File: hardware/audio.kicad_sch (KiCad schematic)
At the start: 35 parts, among them J4 NCJ6FA-H-0, J5 NCJ6FA-H-0, J6 Conn_01x04_Pin, J7 NCJ6FA-H-0, J8 NCJ6FA-H-0, U5 THAT1246, U6 THAT1246, U7 THAT1646, U8 THAT1646

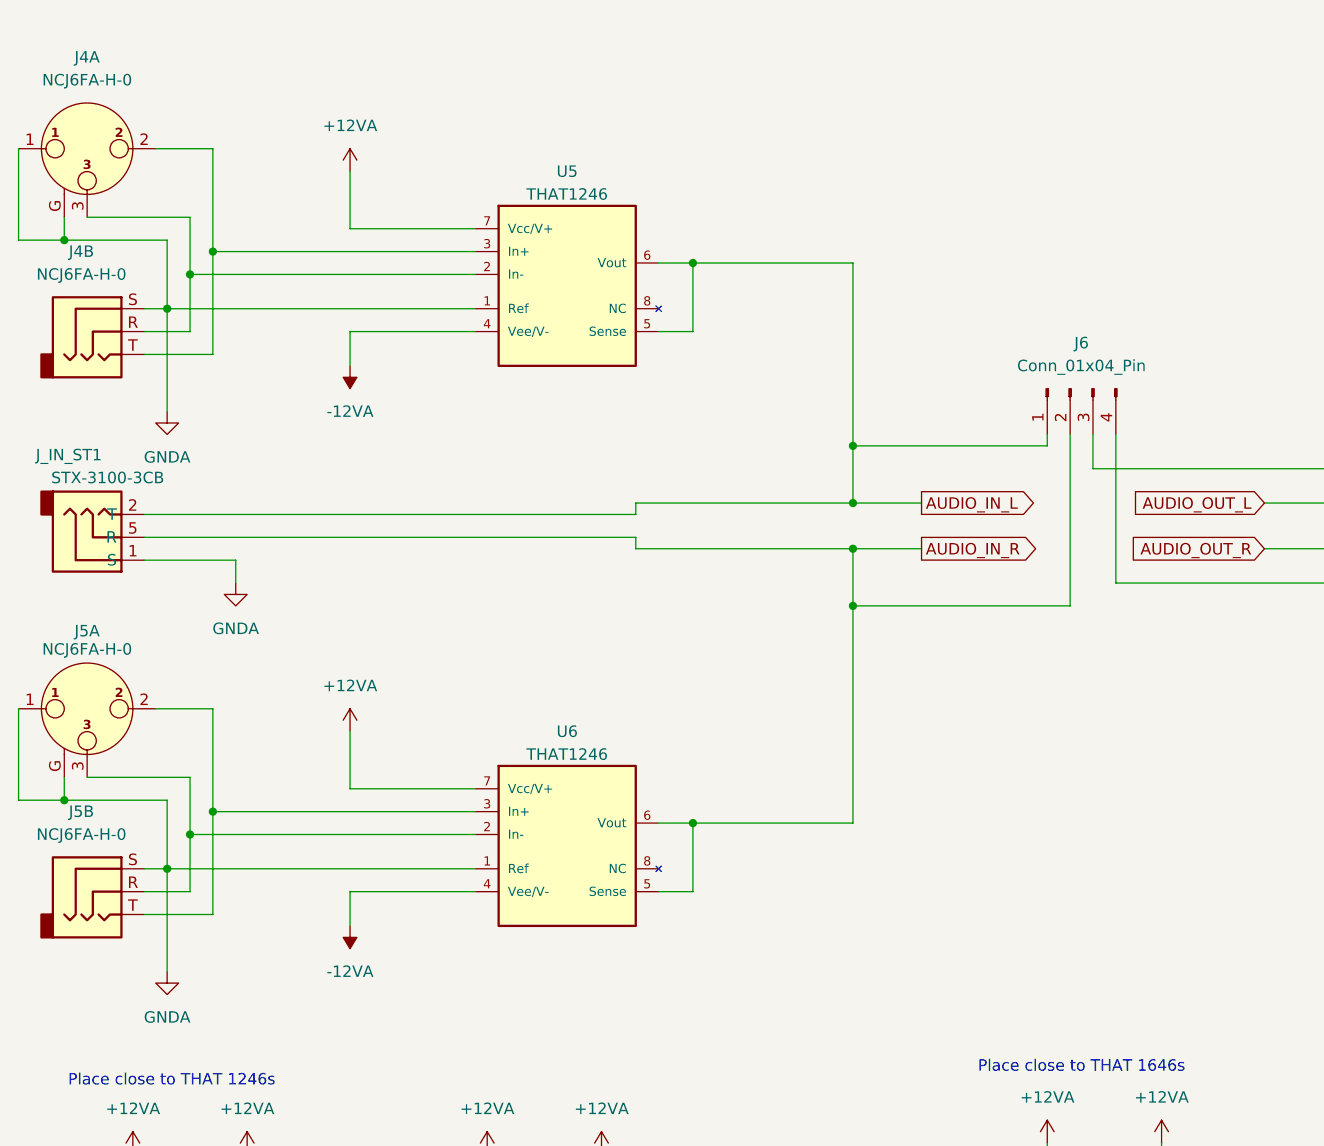
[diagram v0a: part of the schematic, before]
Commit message: simulate and design proper input stage
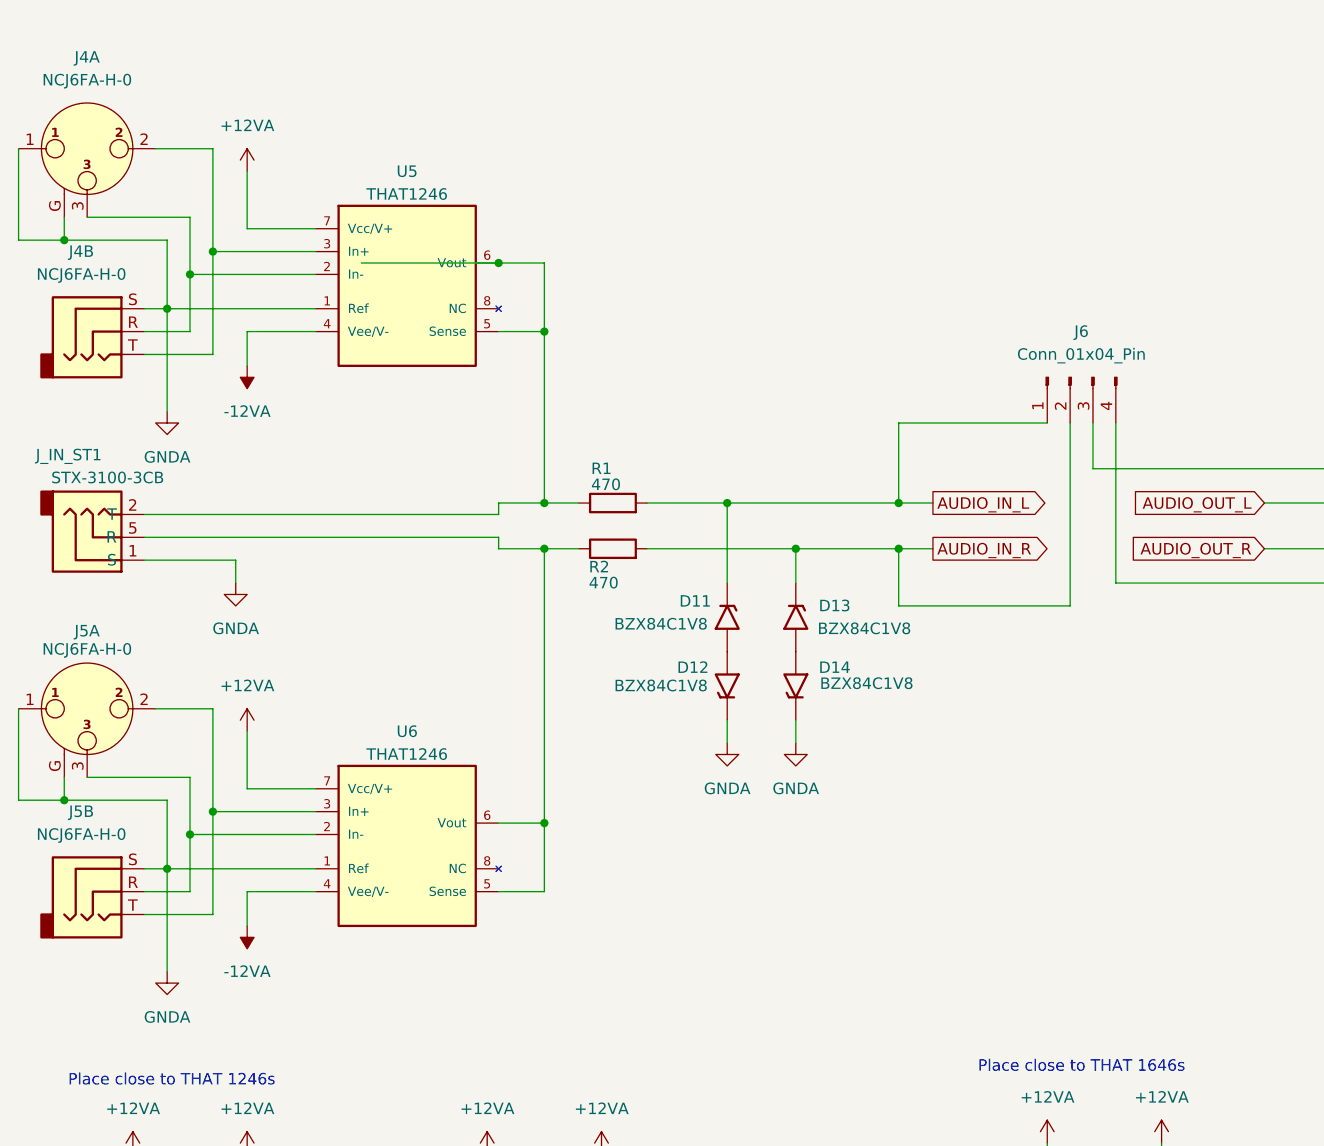
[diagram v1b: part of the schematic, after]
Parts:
- added D11, D12, D13, D14: BZX84C1V8, Diode_SMD:D_SOD-323, symbol Device:D_Zener
- added R1, R2: 470, Resistor_SMD:R_0603_1608Metric, symbol Device:R
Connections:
- net AUDIO_IN_L: now also D11.2 (A), R1.2; no longer J_IN_ST1.2 (T), U5.5 (Sense), U5.6 (Vout)
- net AUDIO_IN_R: now also D13.2 (A), R2.2; no longer J_IN_ST1.5 (R), U6.5 (Sense), U6.6 (Vout)
- net GNDA: now also D12.2 (A), D14.2 (A)
- new net: J_IN_ST1.5 (R), R2.1, U6.5 (Sense), U6.6 (Vout)
- new net: J_IN_ST1.2 (T), R1.1, U5.5 (Sense), U5.6 (Vout)
- new net: D11.1 (K), D12.1 (K)
- new net: D13.1 (K), D14.1 (K)
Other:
- moved on the sheet: J6, U5, U6

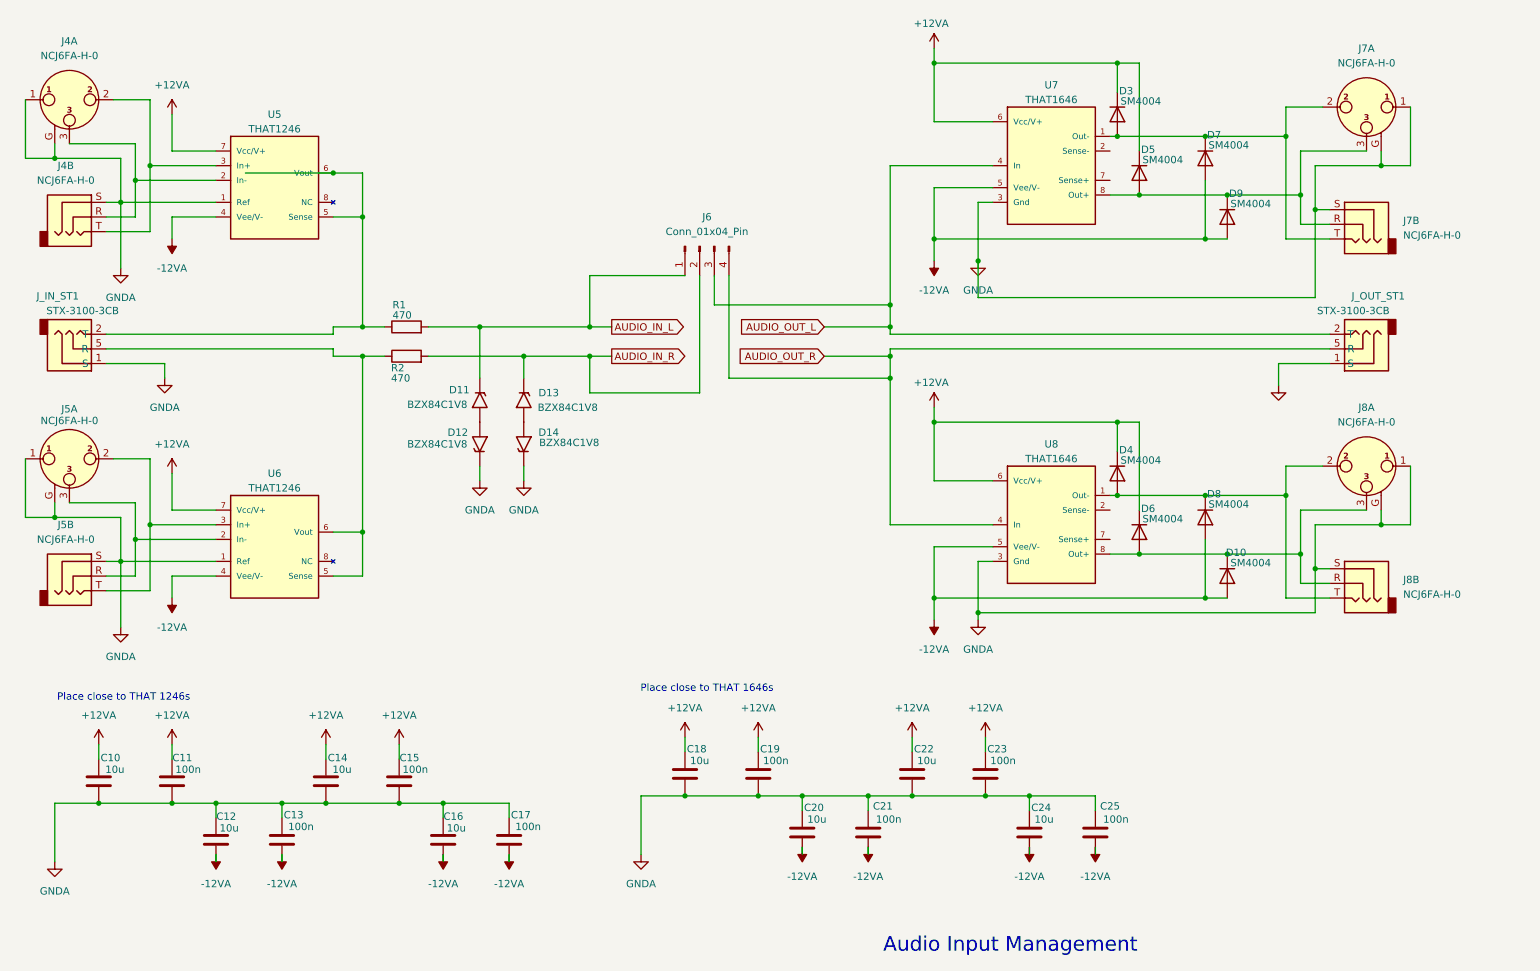
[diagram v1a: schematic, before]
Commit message: cleanup - remove unused schematics
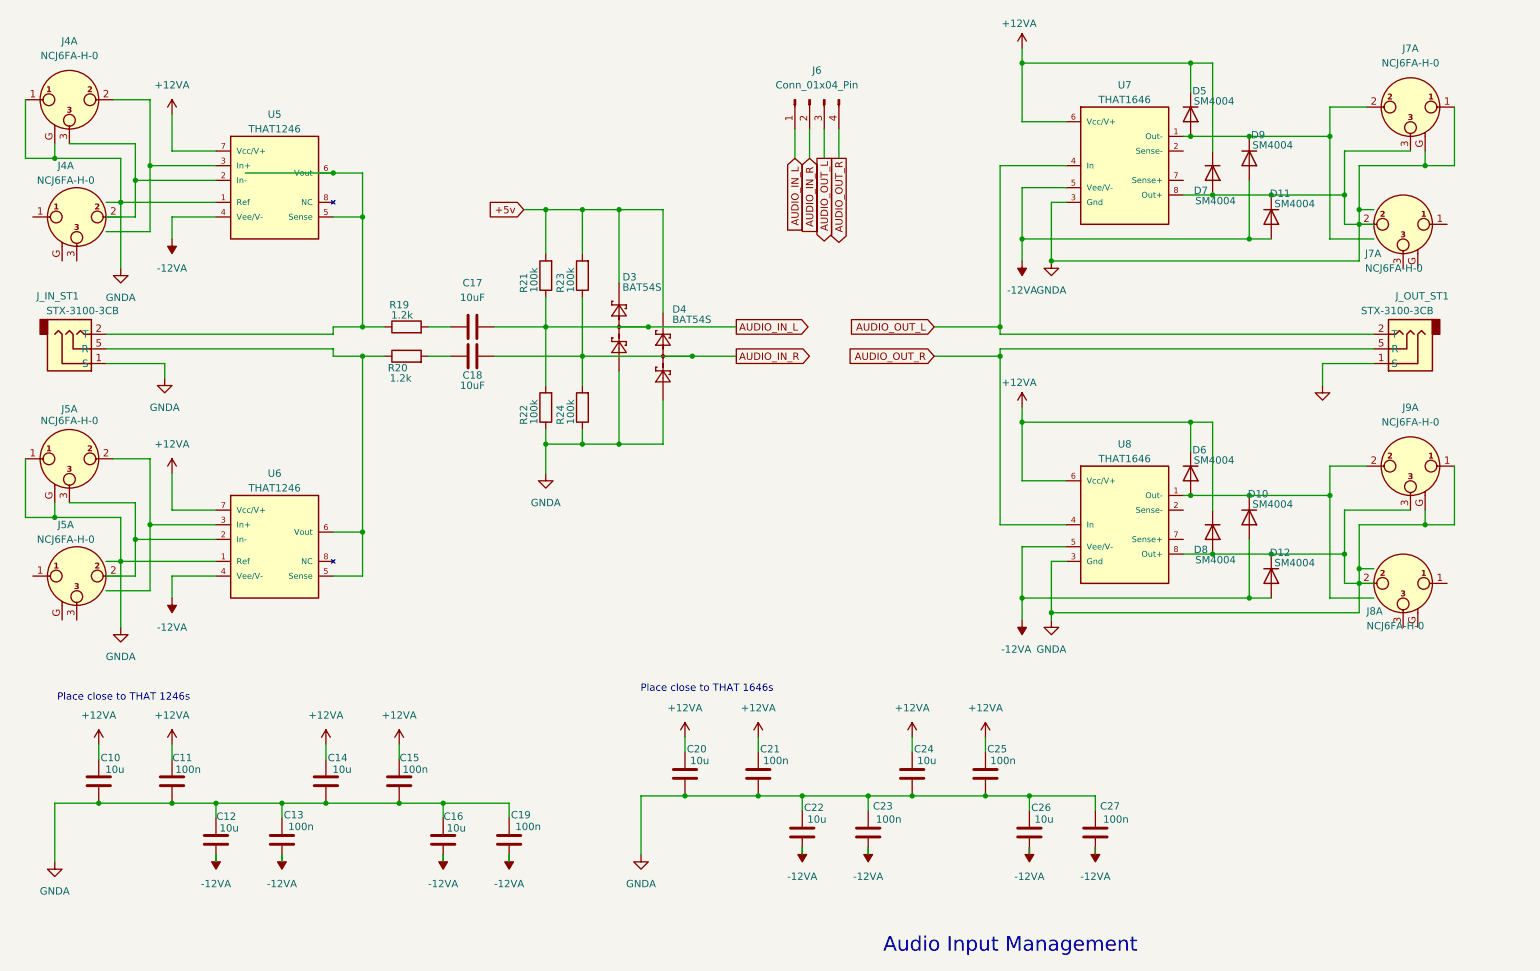
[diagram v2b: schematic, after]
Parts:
- removed D11, D12, D13, D14: BZX84C1V8, Diode_SMD:D_SOD-323, symbol Device:D_Zener
- removed unit 2 of J4
- removed unit 2 of J5
- removed unit 2 of J7
- removed unit 2 of J8
- added C17, C18: 10uF, symbol Device:C
- added D3, D4: BAT54S, Package_TO_SOT_SMD:SOT-23, symbol Diode:BAT54S
- added J4, J5, J7, J8: NCJ6FA-H-0, Connector_Audio:Jack_XLR-6.35mm_Neutrik_NCJ6FA-H-0_Horizontal, symbol Connector_Audio:NCJ6FA-H-0
- added R21, R22, R23, R24: 100k, Resistor_SMD:R_0603_1608Metric, symbol Device:R
- R19: renamed from R1; value 470 -> 1.2k
- R20: renamed from R2; value 470 -> 1.2k
- renumbered C17 to C19, C18 to C20, C19 to C21, C20 to C22, C21 to C23, C22 to C24, C23 to C25, C24 to C26, C25 to C27, D8 to D10, D9 to D11, D10 to D12, D3 to D5, D4 to D6, D5 to D7, D6 to D8, D7 to D9, J8 to J9
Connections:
- net AUDIO_IN_L: now also C17.2, D3.3 (COM), R21.1, R22.2; no longer R19.2
- net AUDIO_IN_R: now also C18.2, D4.3 (COM), R23.1, R24.2; no longer R20.2
- net GNDA: now also D11.1 (K), D12.1 (K), D7.2 (A), D8.2 (A), J7.2, J9.3, U7.8 (Out+), U8.8 (Out+), D3.1 (A), D4.1 (A), J7.1, J7.3, J7.G, J8.2, R22.1, R24.1; no longer J7.1, J7.G
- net at D5.2 (A), D9.1 (K), U7.1 (Out-): now also J7.2; no longer J7.2
- new net: C17.1, R19.2
- new net: C18.1, R20.2
- new net +5v: D3.2 (K), D4.2 (K), R21.2, R23.2
- now unconnected: J7.3
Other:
- moved on the sheet: D10, D11, D12, D5, D6, D7, D8, D9, J6, J7A, J9A, J_OUT_ST1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

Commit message: add protection circuit and repair pcb
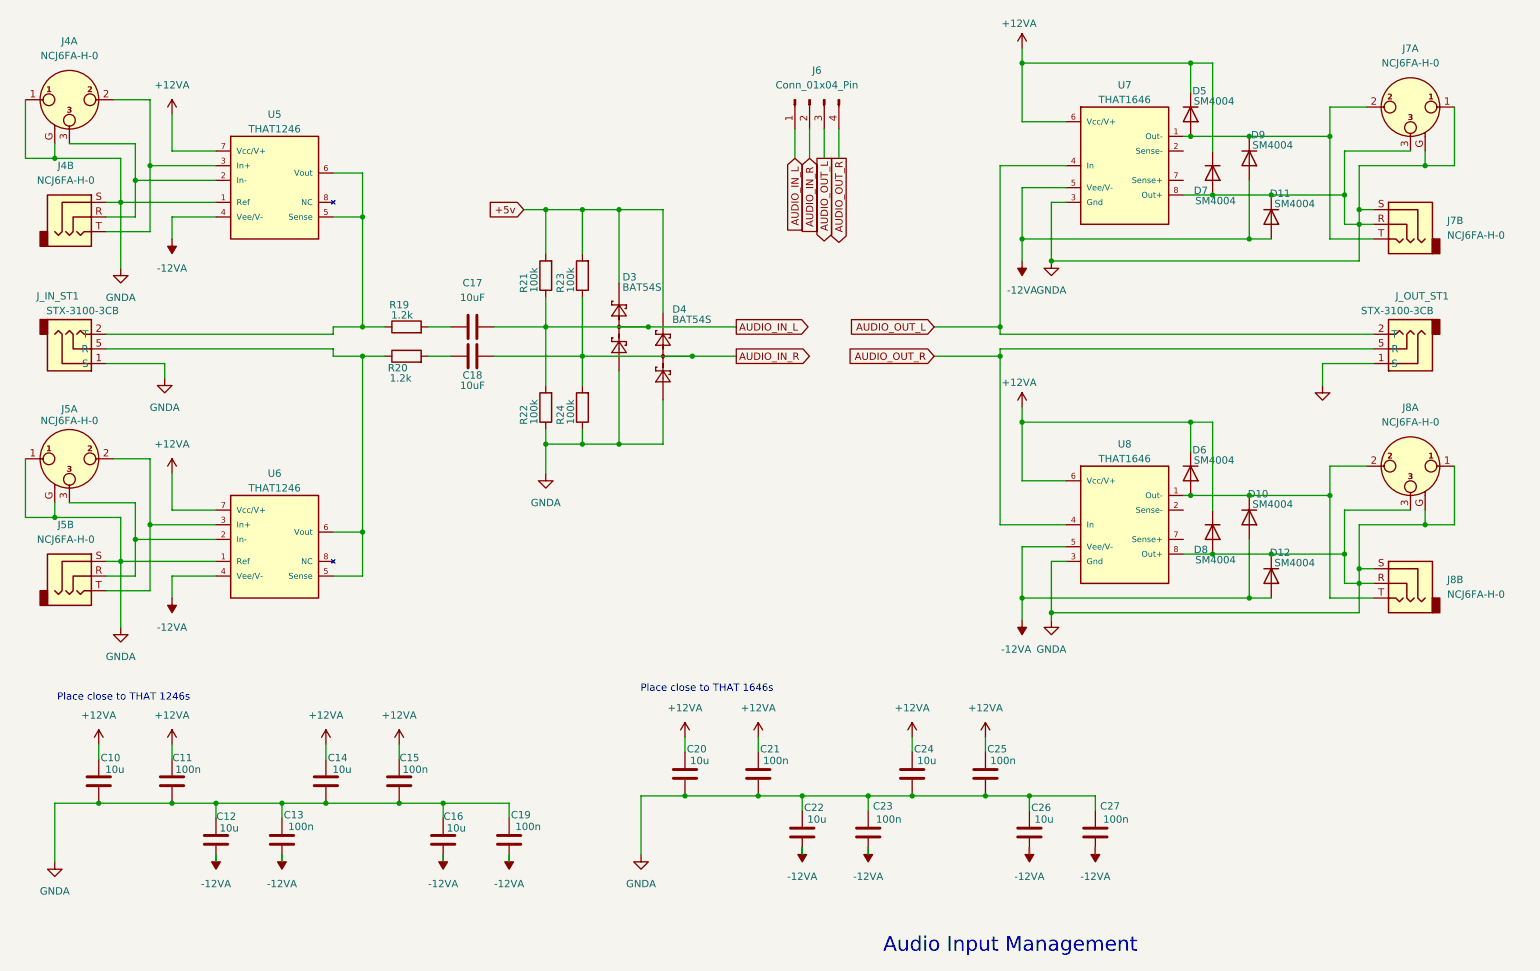
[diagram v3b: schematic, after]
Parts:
- removed J7: NCJ6FA-H-0, Connector_Audio:Jack_XLR-6.35mm_Neutrik_NCJ6FA-H-0_Horizontal, symbol Connector_Audio:NCJ6FA-H-0
- added unit 2 of J7
- renumbered J9 to J8
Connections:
- net GNDA: now also J4.1, J4.G, J4.S, J5.1, J5.G, J5.S, J8.1, J8.3, J8.G, J8.R, J8.S, J7.R, J7.S; no longer J4.1, J4.G, J5.1, J5.G, J8.1, J8.2, J8.3, J8.G
- net at D10.1 (K), D6.2 (A), U8.1 (Out-): now also J8.2, J8.T; no longer J8.2
- net at U6.3 (In+): now also J5.2, J5.T; no longer J5.2
- net at U6.2 (In-): now also J5.3, J5.R; no longer J5.3
- net at U5.3 (In+): now also J4.2, J4.T; no longer J4.2
- net at U5.2 (In-): now also J4.3, J4.R; no longer J4.3
- net at D5.2 (A), D9.1 (K), J7.2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: now also J7.T

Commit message: Add Pad button
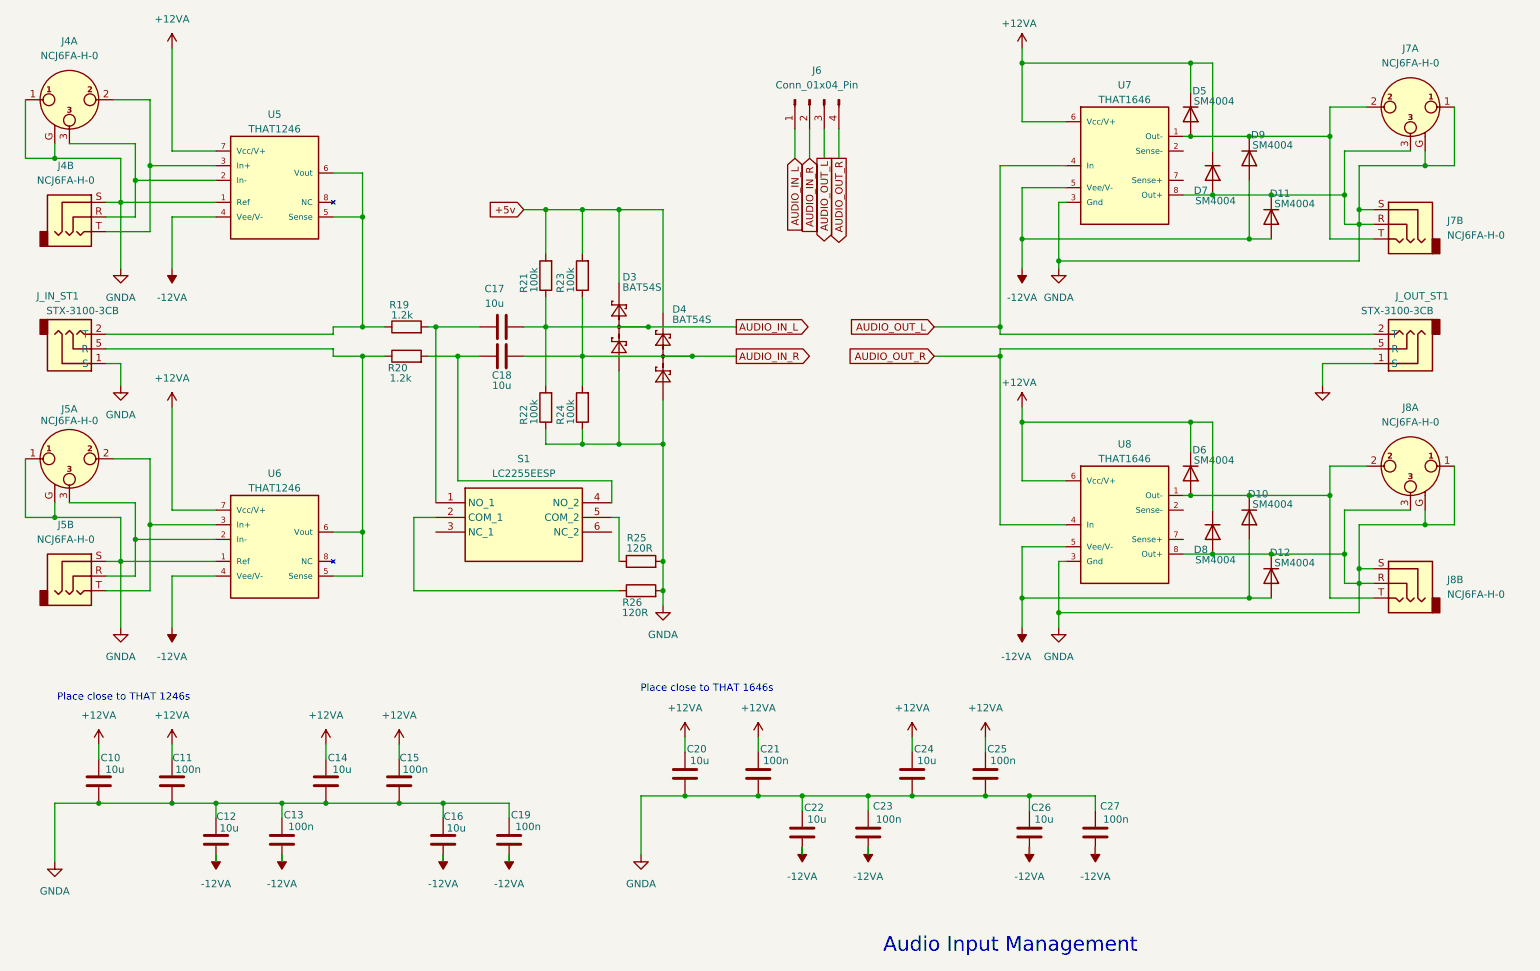
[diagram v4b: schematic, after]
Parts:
- added R25, R26: 120R, Resistor_SMD:R_0603_1608Metric, symbol Device:R
- added S1: LC2255EESP, libs:LC2255EESP, symbol LC2255EESP:LC2255EESP
- C17, C18: value 10uF -> 10u; footprint (none) -> Capacitor_SMD:C_0805_2012Metric
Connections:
- net GNDA: now also R25.2, R26.2
- net at C17.1, R19.2: now also S1.1 (NO_1)
- net at C18.1, R20.2: now also S1.4 (NO_2)
- new net: R26.1, S1.2 (COM_1)
- new net: R25.1, S1.5 (COM_2)
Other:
- moved on the sheet: C17, C18

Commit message: PCB Assembledish Design checks next
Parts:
- added J10, J7: Earth, MountingHole:MountingHole_3.2mm_M3_Pad_Via, symbol Connector_Generic:Conn_01x01
- added JP1: Earth-Gnd Disconnect, Jumper:SolderJumper-2_P1.3mm_Bridged_Pad1.0x1.5mm, symbol Jumper:SolderJumper_2_Bridged
- renumbered J7 to J8, J8 to J9
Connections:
- net GND: now reaches S1.MH1
- net GND: now also C10.2, C11.2, C12.1, C13.1, C14.2, C15.2, C16.1, C19.1, C20.2, C21.2, C22.1, C23.1, C24.2, C25.2, C26.1, C27.1, D3.1 (A), D4.1 (A), J_IN_ST1.1 (S), J_OUT_ST1.1 (S), R22.1, R24.1, R25.2, R26.2, S1.MH2, U5.1 (Ref), U6.1 (Ref), U7.3 (Gnd), U8.3 (Gnd), JP1.1 (A)
- net +5v renamed +5V
- removed net GNDA: C10.2, C11.2, C12.1, C13.1, C14.2, C15.2, C16.1, C19.1, C20.2, C21.2, C22.1, C23.1, C24.2, C25.2, C26.1, C27.1, D11.1 (K), D12.1 (K), D3.1 (A), D4.1 (A), D7.2 (A), D8.2 (A), J4.1, J4.G, J4.S, J5.1, J5.G, J5.S, J8.1, J8.3, J8.G, J8.R, J8.S, J9.1, J9.3, J9.G, J9.R, J9.S, J_IN_ST1.1 (S), J_OUT_ST1.1 (S), R22.1, R24.1, R25.2, R26.2, U5.1 (Ref), U6.1 (Ref), U7.3 (Gnd), U7.8 (Out+), U8.3 (Gnd), U8.8 (Out+)
- new net: D12.1 (K), D8.2 (A), J9.3, J9.R, U8.8 (Out+)
- new net: D11.1 (K), D7.2 (A), J8.3, J8.R, U7.8 (Out+)
- new net Earth: J10.1 (Pin_1), J4.1, J4.G, J4.S, J5.1, J5.G, J5.S, J7.1 (Pin_1), J8.1, J8.G, J8.S, J9.1, J9.G, J9.S, JP1.2 (B)
- no-connect marks 0 -> 6
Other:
- note added: "Place next to star"
- note added: "place close to jacks"
- moved on the sheet: C10, C11, C12, C13, C14, C15, C16, C19, C20, C21, C22, C23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
